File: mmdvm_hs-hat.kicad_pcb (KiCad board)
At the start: 2 copper layers, 65.1 x 30.2 mm, 144 parts, among them P1 I2C, P2 DISPLAY, P3 SMA, P4 STLINK, SW1 DNI, U1 ADF7021, U2 STM32F103C8T6, X1 TCXO, Y1 8MHz

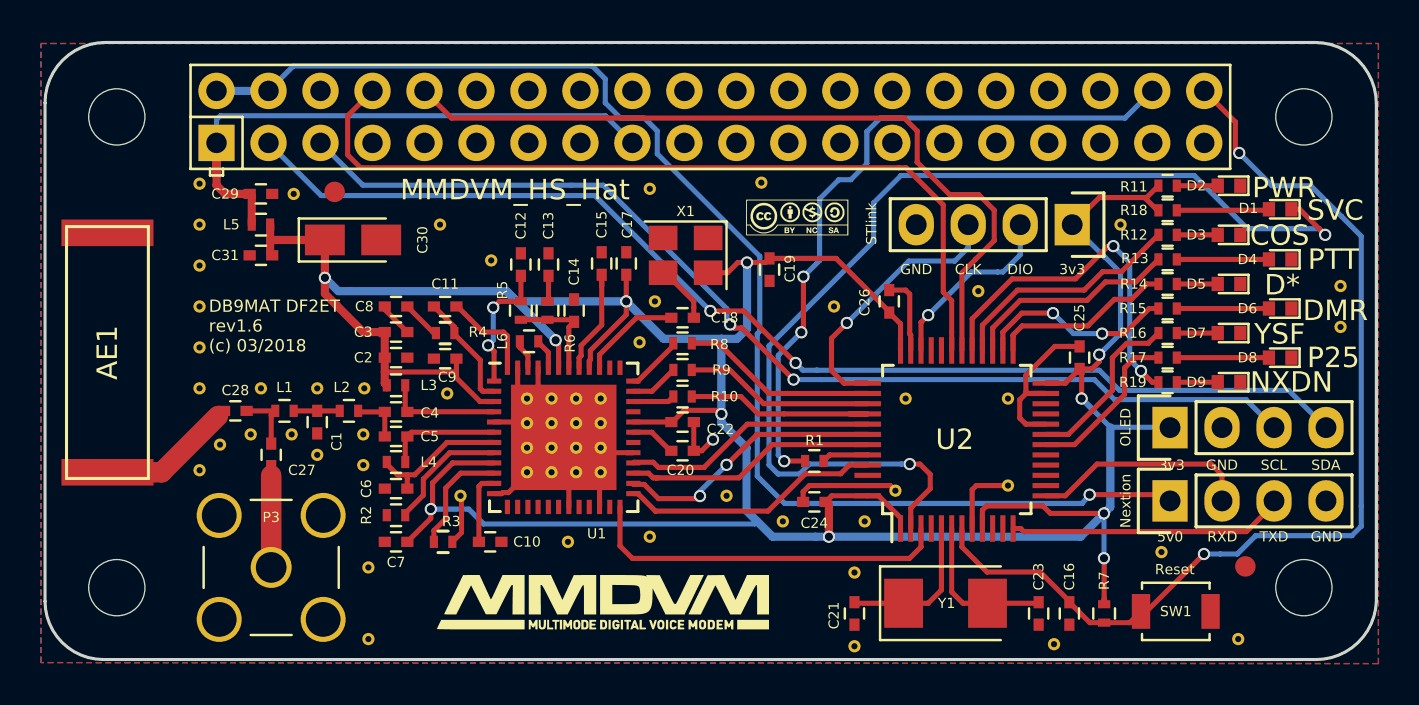
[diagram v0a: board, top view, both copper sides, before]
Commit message: Rotate 180° STLink connector (respect OLED and Nextion orientations). Replace GND pads to VIA (netlist can be safely updated from schematic now). Reroute Service track. Small tweaks to various tracks (WiP). DRC success. Update 3D topview PNG.
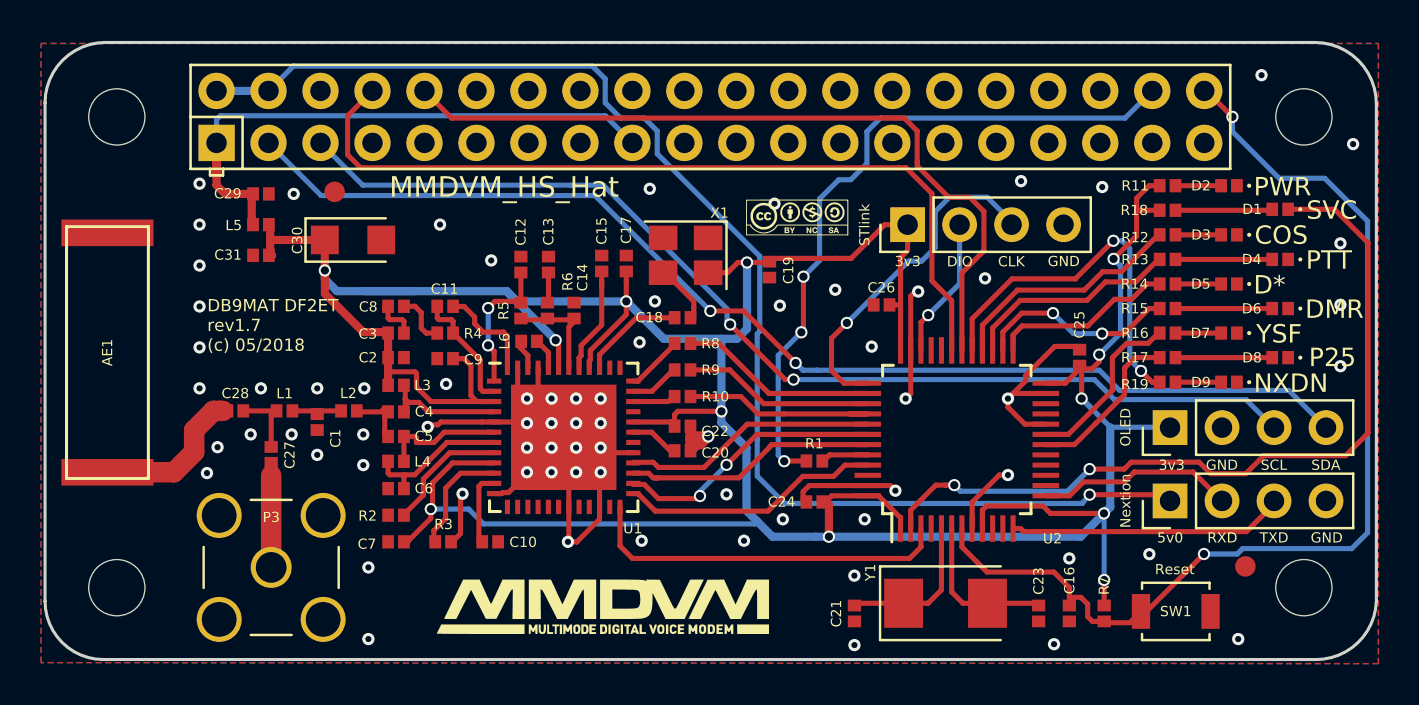
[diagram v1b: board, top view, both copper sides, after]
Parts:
- removed REF** (x62): VIA-0.6mm, MMDVM:VIA-0.6mm
- C1, C10, C11, C12, C13, C14, C15, C16, C17, C18, C19, C2, C20, C21, C22, C23, C24, C25, C26, C27, C28, C29, C3, C31, C4, C5, C6, C7, C8, C9: footprint Capacitors_SMD:C_0402 -> Capacitor_SMD:C_0402_1005Metric
- C30: footprint Capacitors_Tantalum_SMD:CP_Tantalum_Case-A_EIA-3216-18_Reflow -> Capacitor_Tantalum_SMD:CP_EIA-3216-18_Kemet-A
- D1, D2, D3, D4, D5, D6, D7, D8, D9: footprint LEDs:LED_0402 -> LED_SMD:LED_0402_1005Metric
- L1, L2, L3, L4, L5, L6: footprint Inductors_SMD:L_0402 -> Inductor_SMD:L_0402_1005Metric
- P1, P2, P4: footprint Pin_Headers:Pin_Header_Straight_1x04 -> Connector_PinHeader_2.54mm:PinHeader_1x04_P2.54mm_Vertical
- R1, R10, R11, R12, R13, R14, R15, R16, R17, R18, R19, R2, R3, R4, R5, R6, R7, R8, R9: footprint Resistors_SMD:R_0402 -> Resistor_SMD:R_0402_1005Metric
- moved P4 8.04 mm to (197.6, 114.5), turned to 90 degrees
- moved REF*** 1.41 mm to (189.3, 123.7)
- moved C26 0.41 mm to (196.3, 118.4), turned to 180 degrees
- moved G*** 0.22 mm to (182.7, 133.2)
- moved C22 0.20 mm to (186.6, 124.4)
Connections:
- AE1 pad 2: (no net) -> Net-(AE1-Pad2)
- PI1 pad 11: (no net) -> Net-(PI1-Pad11)
- PI1 pad 12: (no net) -> Net-(PI1-Pad12)
- PI1 pad 13: (no net) -> Net-(PI1-Pad13)
- PI1 pad 15: (no net) -> Net-(PI1-Pad15)
- PI1 pad 16: (no net) -> Net-(PI1-Pad16)
- PI1 pad 18: (no net) -> Net-(PI1-Pad18)
- PI1 pad 19: (no net) -> Net-(PI1-Pad19)
- PI1 pad 21: (no net) -> Net-(PI1-Pad21)
- PI1 pad 22: (no net) -> Net-(PI1-Pad22)
- PI1 pad 23: (no net) -> Net-(PI1-Pad23)
- PI1 pad 24: (no net) -> Net-(PI1-Pad24)
- PI1 pad 26: (no net) -> Net-(PI1-Pad26)
- PI1 pad 27: (no net) -> Net-(PI1-Pad27)
- PI1 pad 28: (no net) -> Net-(PI1-Pad28)
- PI1 pad 29: (no net) -> Net-(PI1-Pad29)
- PI1 pad 31: (no net) -> Net-(PI1-Pad31)
- PI1 pad 32: (no net) -> Net-(PI1-Pad32)
- PI1 pad 33: (no net) -> Net-(PI1-Pad33)
- PI1 pad 35: (no net) -> Net-(PI1-Pad35)
- PI1 pad 36: (no net) -> Net-(PI1-Pad36)
- PI1 pad 37: (no net) -> Net-(PI1-Pad37)
- PI1 pad 7: (no net) -> Net-(PI1-Pad7)
- U1 pad 13: (no net) -> Net-(U1-Pad13)
- U1 pad 14: (no net) -> Net-(U1-Pad14)
- U1 pad 15: (no net) -> Net-(U1-Pad15)
- U1 pad 16: (no net) -> Net-(U1-Pad16)
- U1 pad 17: (no net) -> Net-(U1-Pad17)
- U1 pad 18: (no net) -> Net-(U1-Pad18)
- U1 pad 20: (no net) -> Net-(U1-Pad20)
- U1 pad 21: (no net) -> Net-(U1-Pad21)
- U1 pad 23: (no net) -> Net-(U1-Pad23)
- U1 pad 30: (no net) -> Net-(U1-Pad30)
- U1 pad 33: (no net) -> Net-(U1-Pad33)
- U1 pad 37: (no net) -> Net-(U1-Pad37)
- U1 pad 38: (no net) -> Net-(U1-Pad38)
- U2 pad 10: (no net) -> Net-(U2-Pad10)
- U2 pad 11: (no net) -> Net-(U2-Pad11)
- U2 pad 14: (no net) -> Net-(U2-Pad14)
- U2 pad 15: (no net) -> Net-(U2-Pad15)
- U2 pad 16: (no net) -> Net-(U2-Pad16)
- U2 pad 17: (no net) -> Net-(U2-Pad17)
- U2 pad 21: (no net) -> Net-(U2-Pad21)
- U2 pad 22: (no net) -> Net-(U2-Pad22)
- U2 pad 32: (no net) -> Net-(U2-Pad32)
- U2 pad 33: (no net) -> Net-(U2-Pad33)
- U2 pad 4: (no net) -> Net-(U2-Pad4)
- U2 pad 46: (no net) -> Net-(U2-Pad46)
- X1 pad 1: (no net) -> Net-(X1-Pad1)
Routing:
- net SERVICE: track 52.4 -> 39.4 mm
- net GND: track 39.5 -> 50.5 mm, vias 1 -> 73
- net VDD: track 170.5 -> 178.7 mm, vias 11 -> 12
- net SWCLK: track 13.2 -> 16.9 mm
- net SWDIO: track 9.06 -> 6.93 mm
- net NRST: track 49.6 -> 51.4 mm
- net DISP_RXD: track 10.7 -> 9.68 mm
- net Net-(AE1-Pad1): track 6.54 -> 7.55 mm
- net Net-(C8-Pad1): track 1.92 -> 2.61 mm
- net TXD: track 38.7 -> 38.0 mm
- net NXDN_LED: track 17.7 -> 18.3 mm
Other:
- board text added: "DB9MAT DF2ET rev1.7 (c) 05/2018"
- board text removed: "DB9MAT DF2ET rev1.6 (c) 03/2018"
